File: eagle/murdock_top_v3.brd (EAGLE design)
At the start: 47 x 31.8 mm, 35 parts, among them IC1 74HC595D, IC2 74HC595D, X1 MURDOCK_STACK

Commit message: improved pads
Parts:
- moved LED14 1.35 mm to (41.4, 14.5)
- moved R8 1.30 mm to (37.8, 23.5)
- moved R16 1.22 mm to (39.3, 18.3)
- moved LED1 0.84 mm to (41.4, 21.0)
- moved LED16 0.42 mm to (41.4, 25.1)
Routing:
- net LED_C: track 38.8 -> 40.2 mm
- net N$7: track 5.37 -> 4.03 mm
- net QA: track 40.8 -> 39.5 mm
- net Q7: track 27.8 -> 26.6 mm
- net N$9: track 1.85 -> 2.77 mm
- net GND: track 61.1 -> 60.4 mm
- net N$10: track 1.76 -> 2.27 mm

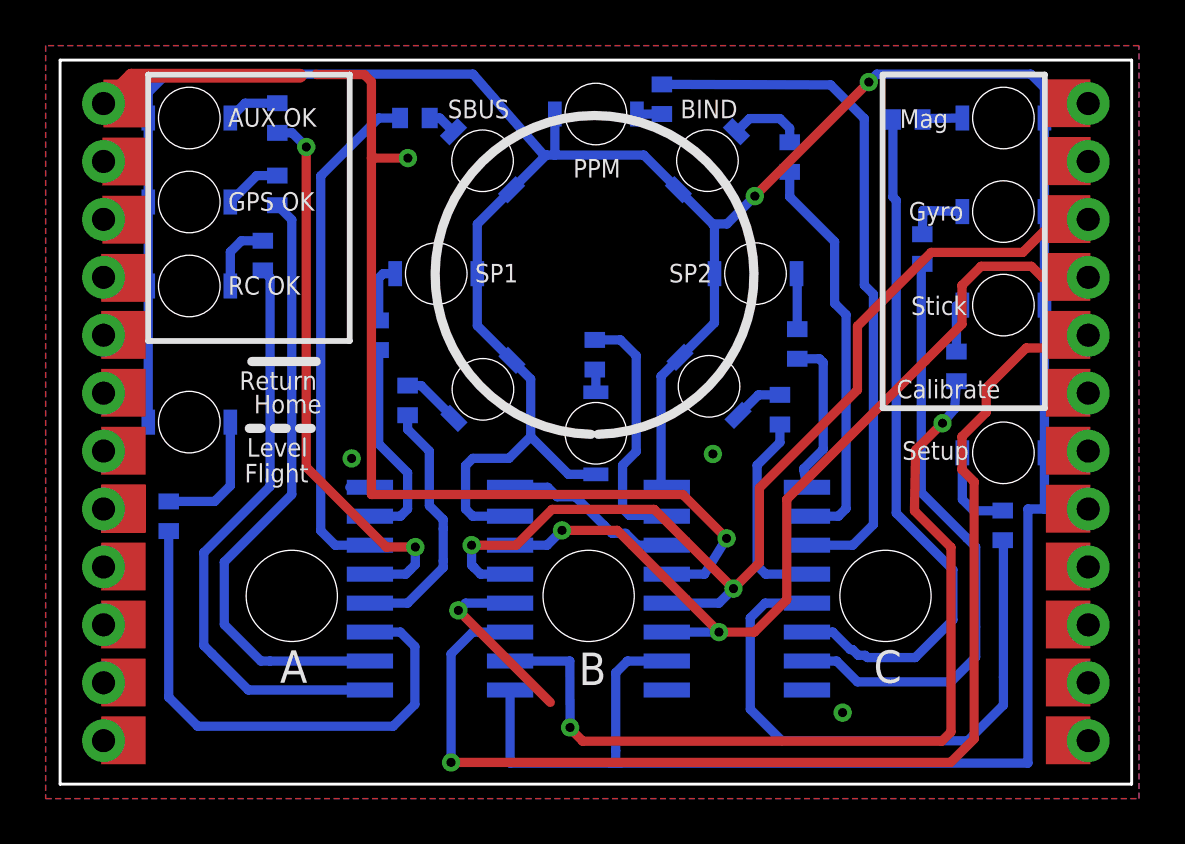
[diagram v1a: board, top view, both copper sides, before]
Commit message: conneced LEDs to switche 3v3
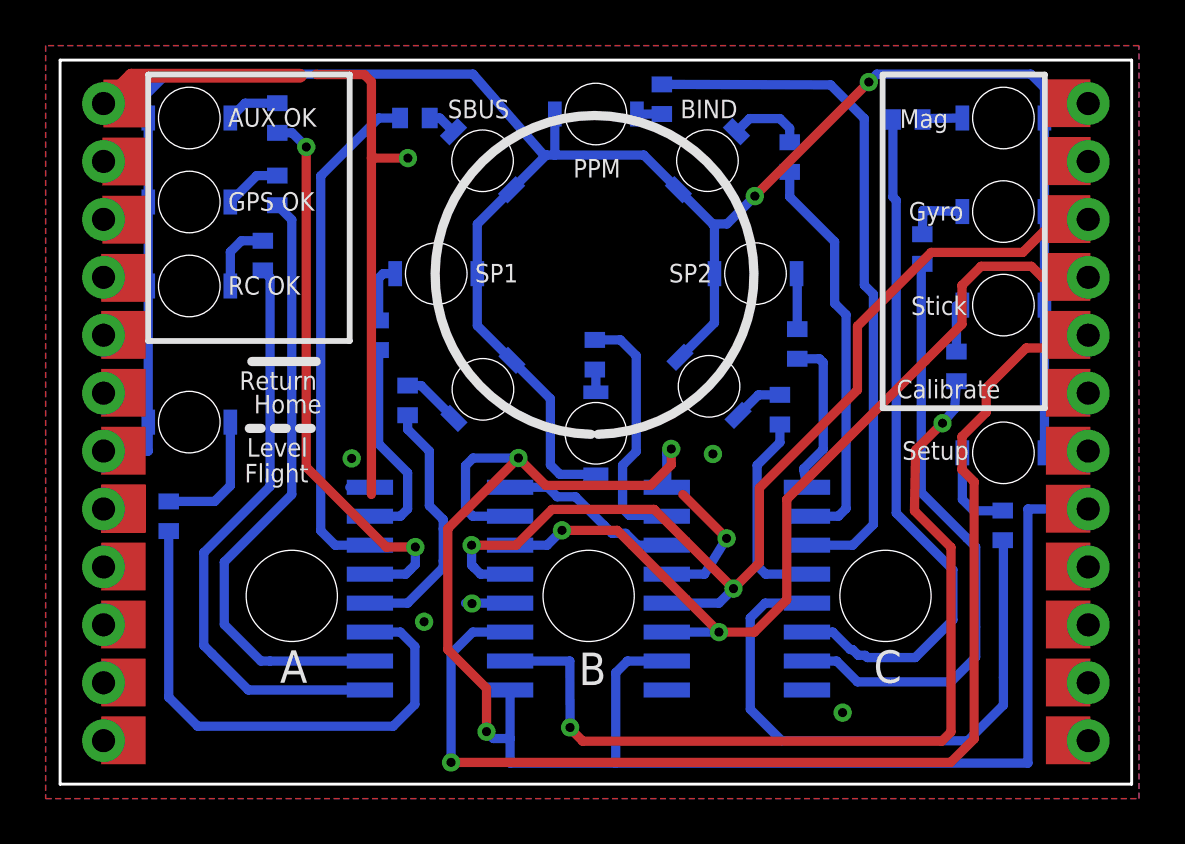
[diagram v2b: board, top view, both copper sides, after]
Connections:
- new net 3V3_SP: LED1.A, LED10.A, LED11.A, LED12.A, LED13.A, LED14.A, LED15.A, LED16.A, LED2.A, LED3.A, LED4.A, LED5.A, LED6.A, LED7.A, LED8.A, LED9.A, X1.3V3_SP
- net 3.3V: no longer LED1.A, LED10.A, LED11.A, LED12.A, LED13.A, LED14.A, LED15.A, LED16.A, LED2.A, LED3.A, LED4.A, LED5.A, LED6.A, LED7.A, LED8.A, LED9.A
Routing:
- net 3V3_SP: track 0.00 -> 104.7 mm, vias 0 -> 2
- net 3.3V: track 164.7 -> 77.7 mm, vias 2 -> 3
- net GND: track 60.4 -> 40.6 mm, vias 6 -> 7

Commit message: more led names
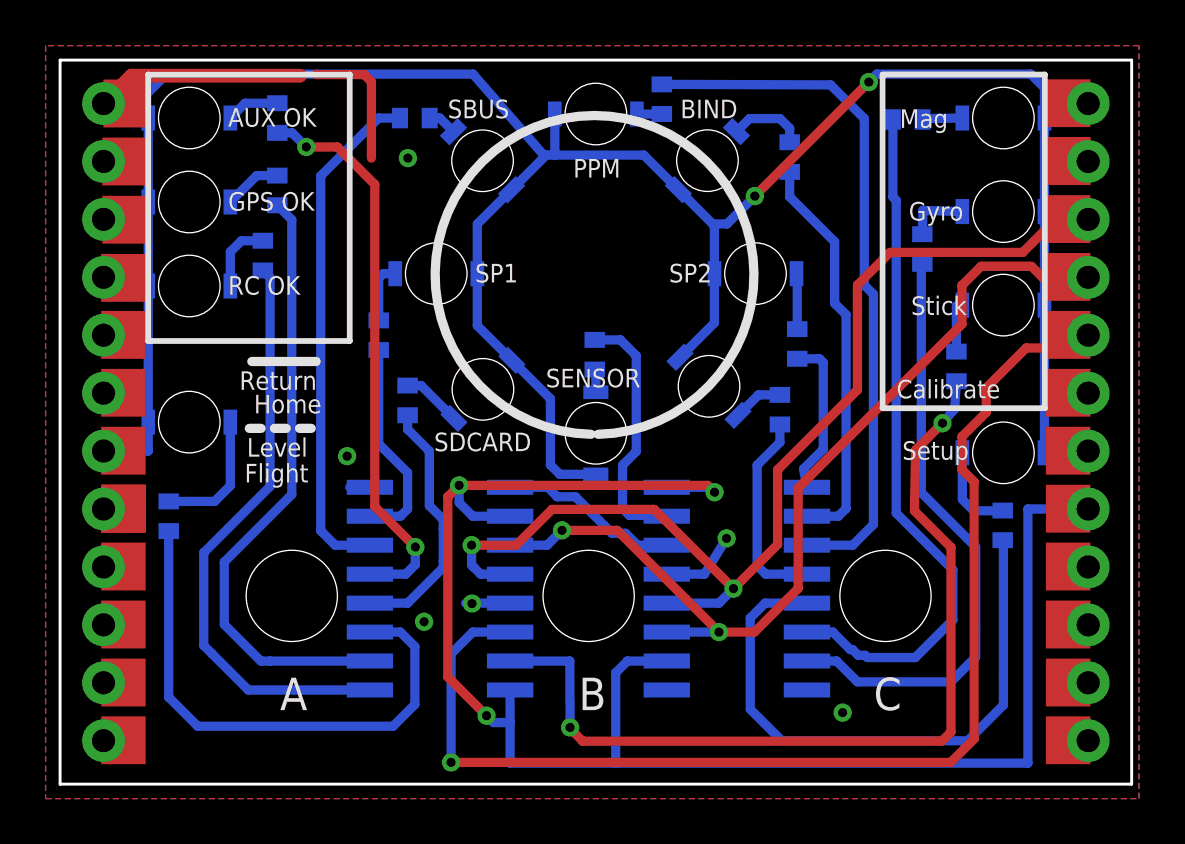
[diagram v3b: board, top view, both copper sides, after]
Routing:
- net GND: track 40.6 -> 21.5 mm, vias 7 -> 6
- net 3.3V: track 77.7 -> 75.0 mm
- net LED_L: track 45.3 -> 46.4 mm
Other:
- board text added: "SDCARD"
- board text added: "SENSOR"

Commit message: merge
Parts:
- moved R15 3.41 mm to (9.14, 19.8)
- moved R14 1.16 mm to (9.38, 24.9)
- moved LED2 0.50 mm to (6.17, 21.8)
- moved LED3 0.50 mm to (6.17, 25.5)
- moved LED4 0.50 mm to (6.17, 15.9)
- moved LED6 0.50 mm to (6.17, 29.2)
- moved LED1 0.40 mm to (41.0, 21.0)
- moved LED14 0.40 mm to (41.0, 14.5)
- moved LED15 0.40 mm to (41.0, 29.2)
- moved LED16 0.40 mm to (41.0, 25.1)
- moved R11 0.18 mm to (9.69, 29.3), turned to 0 degrees
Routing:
- net QB: track 25.9 -> 22.5 mm
- net N$15: track 2.33 -> 1.14 mm
- net 3V3_SP: track 104.7 -> 105.9 mm
- net N$12: track 2.54 -> 1.42 mm
- net LED_L: track 46.4 -> 45.3 mm
- net QC: track 26.9 -> 26.3 mm
- net N$11: track 3.12 -> 2.59 mm
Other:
- board text added: "SD CARD"
- board text removed: "SDCARD"
